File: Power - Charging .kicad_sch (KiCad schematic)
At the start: 10 parts, among them U3 MP2667GG-0000-Z

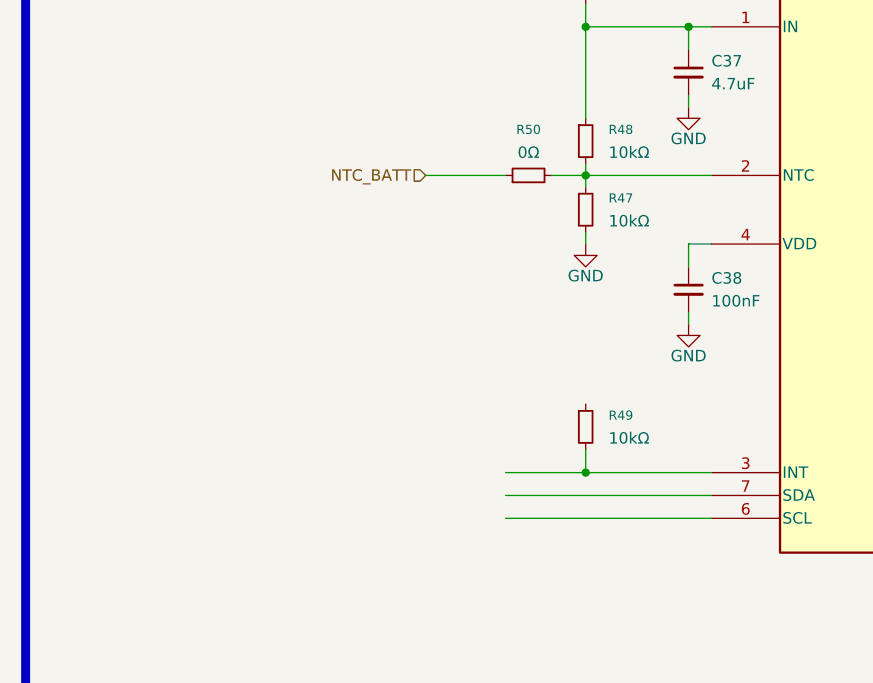
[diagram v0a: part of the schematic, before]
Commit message: charging int and i2c
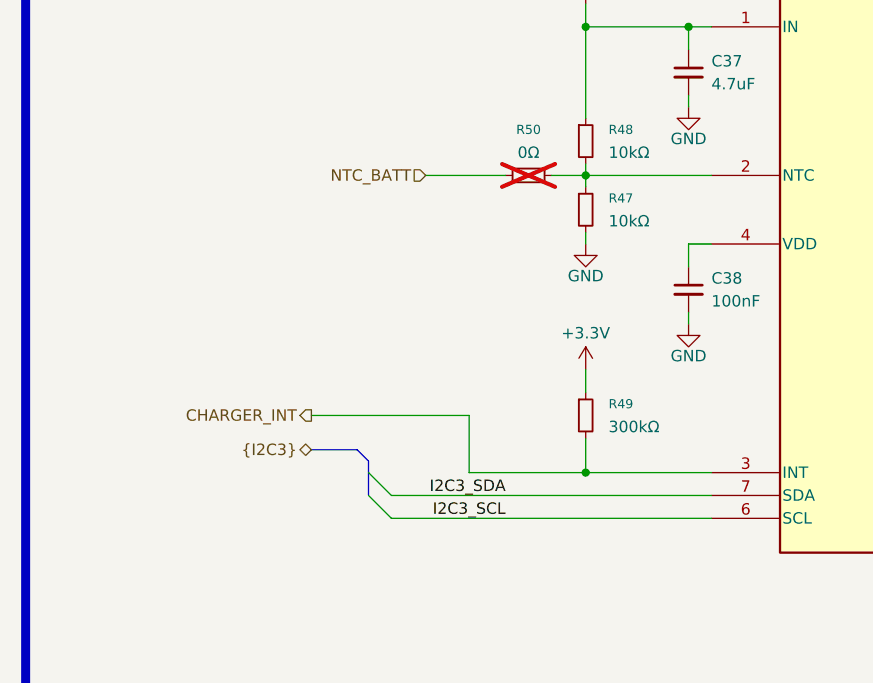
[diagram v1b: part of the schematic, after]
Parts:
- removed R49: 10kΩ, 0_resistors:R_0402_1005Metric, symbol 0_resistors:0402WGF1002TCE
- added R49: 300kΩ, 0_resistors:R_0603_1608Metric, symbol 0_resistors:0603WAF3003T5E
- R50: now not fitted; now left out of the parts list
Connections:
- net CHARGER_INT: now reaches U3.3 (INT)
- net CHARGER_INT: now also R49.2
- net I2C3_SCL: now reaches U3.6 (SCL)
- net I2C3_SDA: now reaches U3.7 (SDA)
- new net +3.3V: R49.1

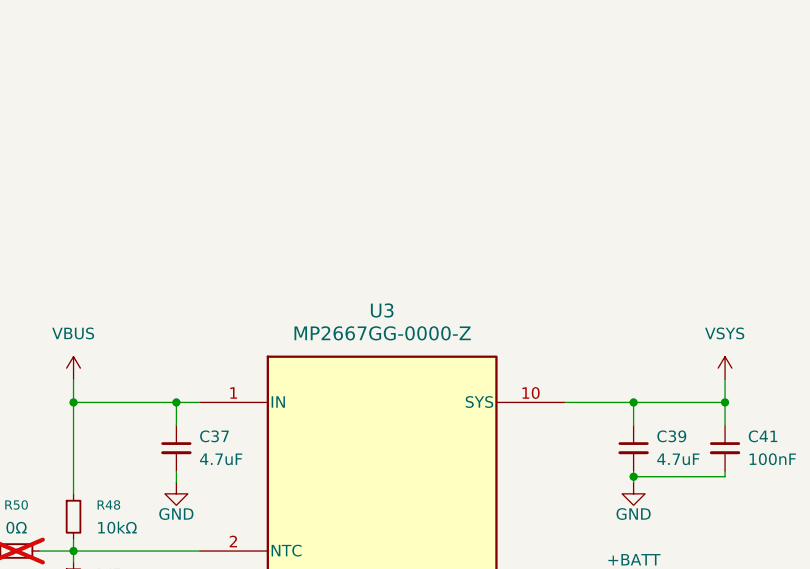
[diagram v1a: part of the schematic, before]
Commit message: added power jumper to bypass charger
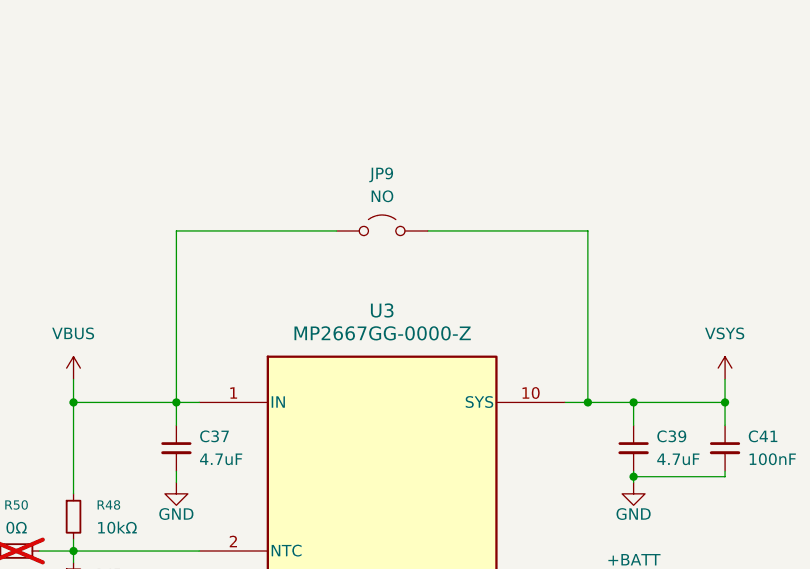
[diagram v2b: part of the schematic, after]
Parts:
- added JP9: NO, Jumper:SolderJumper-2_P1.3mm_Open_TrianglePad1.0x1.5mm, symbol 0_modules:Jumper_2_Open
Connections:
- net VBUS: now also JP9.1 (A)
- net VSYS: now also JP9.2 (B)
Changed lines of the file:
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@@
+		(color 0 0 0 0)
+	)
+	(junction
+		(at 234.95 97.79)
+		(diameter 0)
 		(color 0 0 0 0)
 	)
@@
 	(wire
 		(pts
+			(xy 234.95 78.74) (xy 234.95 97.79)
+		)
+		(stroke
+			(width 0)
+			(type default)
+		)
+	)
+	(wire
+		(pts
 			(xy 164.846 140.97) (xy 164.846 147.32)
 		)
@@
 	(wire
 		(pts
+			(xy 234.95 78.74) (xy 217.17 78.74)
+		)
+		(stroke
+			(width 0)
+			(type default)
+		)
+	)
+	(wire
+		(pts
 			(xy 177.8 114.3) (xy 177.8 115.57)
 		)
@@
 		)
 	)
+	(wire
+		(pts
+			(xy 189.23 78.74) (xy 207.01 78.74)
+		)
+		(stroke
+			(width 0)
+			(type default)
+		)
+	)
 	(bus
 		(pts
@@
 	(wire
 		(pts
+			(xy 234.95 97.79) (xy 240.03 97.79)
+		)
+		(stroke
+			(width 0)
+			(type default)
+		)
+	)
+	(wire
+		(pts
 			(xy 177.8 120.65) (xy 177.8 121.92)
 		)
@@
 	(wire
 		(pts
-			(xy 232.41 97.79) (xy 240.03 97.79)
+			(xy 232.41 97.79) (xy 234.95 97.79)
 		)
 		(stroke
@@
 		(pts
 			(xy 177.8 147.32) (xy 177.8 143.51)
+		)
+		(stroke
+			(width 0)
+			(type default)
+		)
+	)
+	(wire
+		(pts
+			(xy 189.23 78.74) (xy 189.23 97.79)
 		)
 		(stroke
@@
 					(unit 1)
 				)
+			)
+		)
+	)
+	(symbol
+		(lib_id "0_modules:Jumper_2_Open")
+		(at 212.09 78.74 0)
+		(unit 1)
+		(exclude_from_sim no)
+		(in_bom yes)
+		(on_board yes)
+		(dnp no)
+		(fields_autoplaced yes)
+		(property "Reference" "JP9"
+			(at 212.09 72.39 0)
+			(effects
+				(font
+					(size 1.27 1.27)
+				)
+			)
+		)
+		(property "Value" "NO"
+			(at 212.09 74.93 0)
+			(effects
+				(font
+					(size 1.27 1.27)
+				)
+			)
+		)
+		(property "Footprint" "Jumper:SolderJumper-2_P1.3mm_Open_TrianglePad1.0x1.5mm"
+			(at 212.09 78.74 0)
+			(effects
+				(font
+					(size 1.27 1.27)
+				)
+				(hide yes)
+			)
+		)
+		(property "Datasheet" "~"
+			(at 212.09 78.74 0)
+			(effects
+				(font
+					(size 1.27 1.27)
+				)
+				(hide yes)
+			)
+		)
+		(property "Description" "Jumper, 2-pole, open"
+			(at 212.09 78.74 0)
+			(effects
+				(font
+					(size 1.27 1.27)
+				)
+				(hide yes)
+			)
+		)
+		(pin "2"
+		)
+		(pin "1"
+		)
+		(instances
+			(project "transmitter"
+				(path "/0650c7a8-acba-429c-9f8e-eec0baf0bc1c/fede4c36-00cc-4d3d-b71c-5243ba232202/8a7ea2de-b793-4d09-a9a9-63f506951dfd"
+					(reference "JP9")
+					(unit 1)
+				)

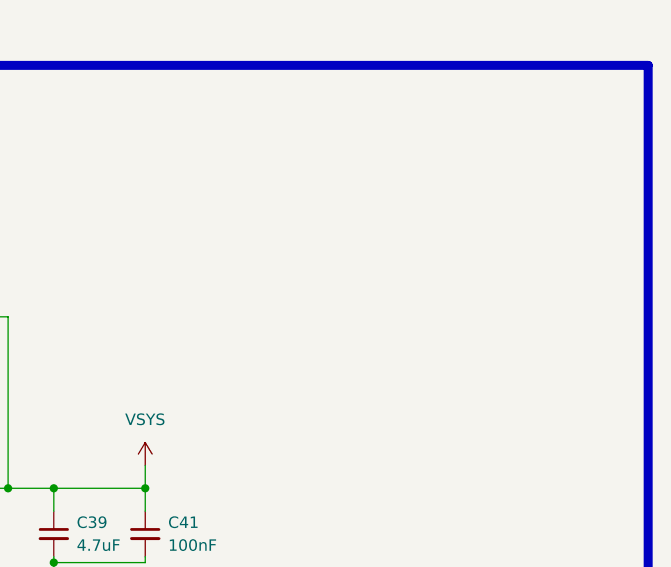
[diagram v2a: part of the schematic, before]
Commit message: added jumper to connect vbat directly to vsys
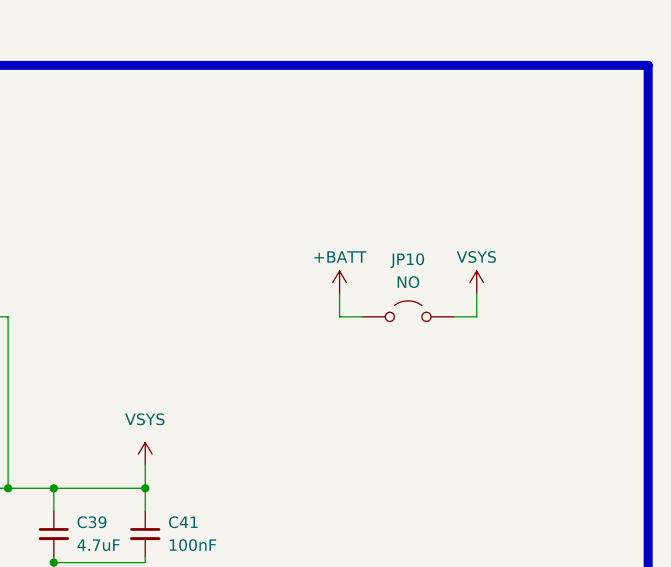
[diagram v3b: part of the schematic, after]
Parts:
- added JP10: NO, Jumper:SolderJumper-2_P1.3mm_Open_TrianglePad1.0x1.5mm, symbol 0_modules:Jumper_2_Open
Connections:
- net +BATT: now also JP10.1 (A)
- net VSYS: now also JP10.2 (B)
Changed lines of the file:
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@@
+	(wire
+		(pts
+			(xy 271.78 78.74) (xy 274.32 78.74)
+		)
+		(stroke
+			(width 0)
+			(type default)
+		)
+	)
 	(wire
 		(pts
@@
 	(wire
 		(pts
+			(xy 271.78 76.2) (xy 271.78 78.74)
+		)
+		(stroke
+			(width 0)
+			(type default)
+		)
+	)
+	(wire
+		(pts
 			(xy 240.03 123.19) (xy 240.03 127)
 		)
@@
 	(wire
 		(pts
+			(xy 287.02 76.2) (xy 287.02 78.74)
+		)
+		(stroke
+			(width 0)
+			(type default)
+		)
+	)
+	(wire
+		(pts
 			(xy 156.21 152.4) (xy 191.77 152.4)
 		)
@@
 		(pts
 			(xy 232.41 152.4) (xy 240.03 152.4)
+		)
+		(stroke
+			(width 0)
+			(type default)
+		)
+	)
+	(wire
+		(pts
+			(xy 284.48 78.74) (xy 287.02 78.74)
 		)
 		(stroke
@@
 	)
 	(symbol
+		(lib_id "0_power_symbols:VSYS")
+		(at 287.02 76.2 0)
+		(unit 1)
+		(exclude_from_sim no)
+		(in_bom yes)
+		(on_board yes)
+		(dnp no)
+		(property "Reference" "#PWR0172"
+			(at 287.02 80.01 0)
+			(effects
+				(font
+					(size 1.27 1.27)
+				)
+				(hide yes)
+			)
+		)
+		(property "Value" "VSYS"
+			(at 287.02 72.136 0)
+			(effects
+				(font
+					(size 1.27 1.27)
+				)
+			)
+		)
+		(property "Footprint" ""
+			(at 287.02 76.2 0)
+			(effects
+				(font
+					(size 1.27 1.27)
+				)
+				(hide yes)
+			)
+		)
+		(property "Datasheet" ""
+			(at 287.02 76.2 0)
+			(effects
+				(font
+					(size 1.27 1.27)
+				)
+				(hide yes)
+			)
+		)
+		(property "Description" "Power symbol creates a global label with name \"VSYS\""
+			(at 287.02 76.2 0)
+			(effects
+				(font
+					(size 1.27 1.27)
+				)
+				(hide yes)
+			)
+		)
+		(pin "1"
+		)
+		(instances
+			(project "transmitter"
+				(path "/0650c7a8-acba-429c-9f8e-eec0baf0bc1c/fede4c36-00cc-4d3d-b71c-5243ba232202/8a7ea2de-b793-4d09-a9a9-63f506951dfd"
+					(reference "#PWR0172")
+					(unit 1)
+				)
+			)
+		)
+	)
+	(symbol
 		(lib_id "0_capacitors:CL21A475KAQNNNE")
 		(at 240.03 102.87 0)
@@
 	)
 	(symbol
+		(lib_id "power:+BATT")
+		(at 271.78 76.2 0)
+		(unit 1)
+		(exclude_from_sim no)
+		(in_bom yes)
+		(on_board yes)
+		(dnp no)
+		(property "Reference" "#PWR0171"
+			(at 271.78 80.01 0)
+			(effects
+				(font
+					(size 1.27 1.27)
+				)
+				(hide yes)
+			)
+		)
+		(property "Value" "+BATT"
+			(at 271.78 72.136 0)
+			(effects
+				(font
+					(size 1.27 1.27)
+				)
+			)
+		)
+		(property "Footprint" ""
+			(at 271.78 76.2 0)
+			(effects
+				(font
+					(size 1.27 1.27)
+				)
+				(hide yes)
+			)
+		)
+		(property "Datasheet" ""
+			(at 271.78 76.2 0)
+			(effects
+				(font
+					(size 1.27 1.27)
+				)
+				(hide yes)
+			)
+		)
+		(property "Description" "Power symbol creates a global label with name \"+BATT\""
+			(at 271.78 76.2 0)
+			(effects
+				(font
+					(size 1.27 1.27)
+				)
+				(hide yes)
+			)
+		)
+		(pin "1"
+		)
+		(instances
+			(project "transmitter"
+				(path "/0650c7a8-acba-429c-9f8e-eec0baf0bc1c/fede4c36-00cc-4d3d-b71c-5243ba232202/8a7ea2de-b793-4d09-a9a9-63f506951dfd"
+					(reference "#PWR0171")
+					(unit 1)
+				)
+			)
+		)
+	)
+	(symbol
 		(lib_id "power:GND")
 		(at 177.8 121.92 0)
@@
 					(unit 1)
 				)
+			)
+		)
+	)
+	(symbol
+		(lib_id "0_modules:Jumper_2_Open")
+		(at 279.4 78.74 0)
+		(unit 1)
+		(exclude_from_sim no)
+		(in_bom yes)
+		(on_board yes)
+		(dnp no)
+		(fields_autoplaced yes)
+		(property "Reference" "JP10"
+			(at 279.4 72.39 0)
+			(effects
+				(font
+					(size 1.27 1.27)
+				)
+			)
+		)
+		(property "Value" "NO"
+			(at 279.4 74.93 0)
+			(effects
+				(font
+					(size 1.27 1.27)
+				)
+			)
+		)
+		(property "Footprint" "Jumper:SolderJumper-2_P1.3mm_Open_TrianglePad1.0x1.5mm"
+			(at 279.4 78.74 0)
+			(effects
+				(font
+					(size 1.27 1.27)
+				)
+				(hide yes)
+			)
+		)
+		(property "Datasheet" "~"
+			(at 279.4 78.74 0)
+			(effects
+				(font
+					(size 1.27 1.27)
+				)
+				(hide yes)
+			)
+		)
+		(property "Description" "Jumper, 2-pole, open"
+			(at 279.4 78.74 0)
+			(effects
+				(font
+					(size 1.27 1.27)
+				)
+				(hide yes)
+			)
+		)
+		(pin "2"
+		)
+		(pin "1"
+		)
+		(instances
+			(project "transmitter"
+				(path "/0650c7a8-acba-429c-9f8e-eec0baf0bc1c/fede4c36-00cc-4d3d-b71c-5243ba232202/8a7ea2de-b793-4d09-a9a9-63f506951dfd"
+					(reference "JP10")
+					(unit 1)
+				)

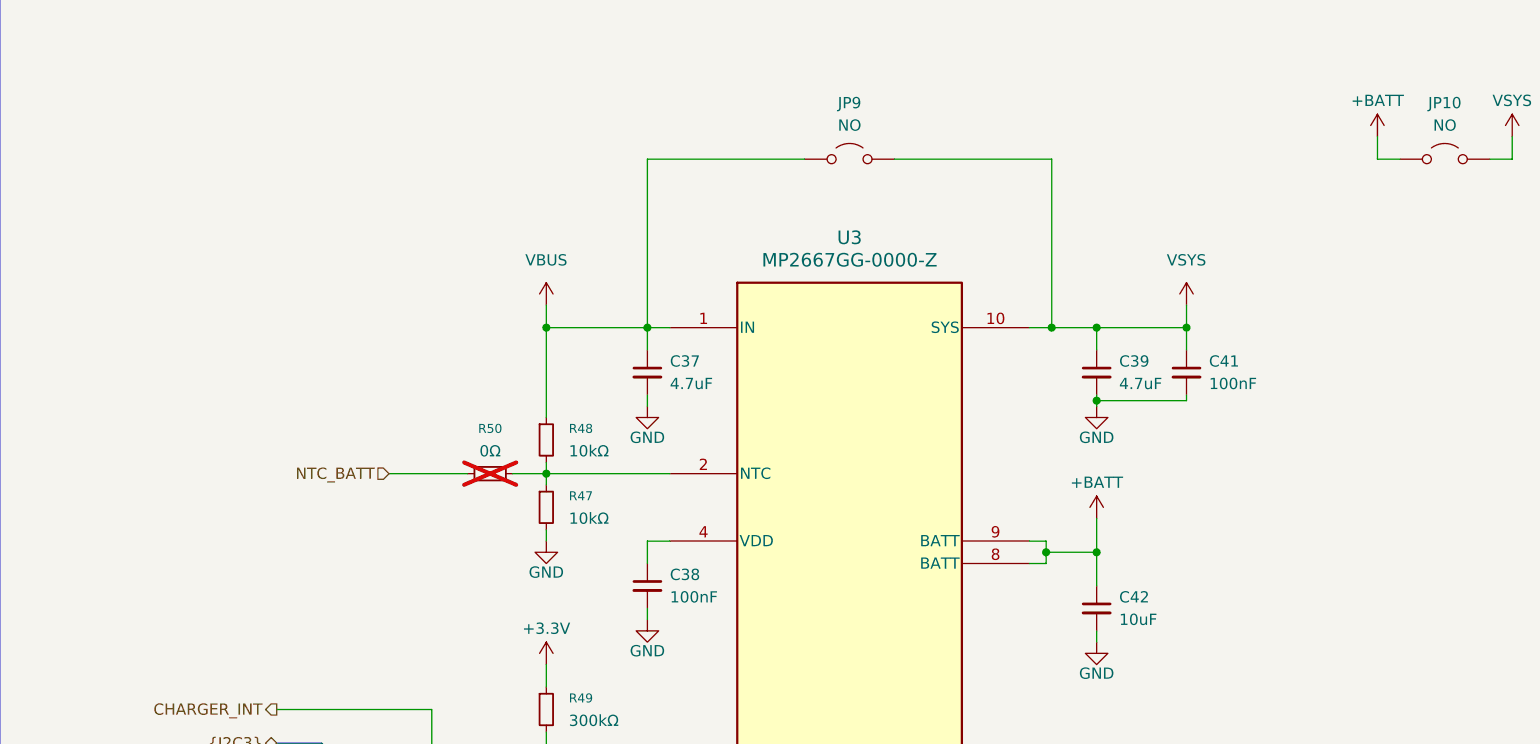
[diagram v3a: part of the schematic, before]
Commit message: duzo zmian, layout przetwornic i zasilania, wstepny routing sd card impedance control, usb differential impedance control
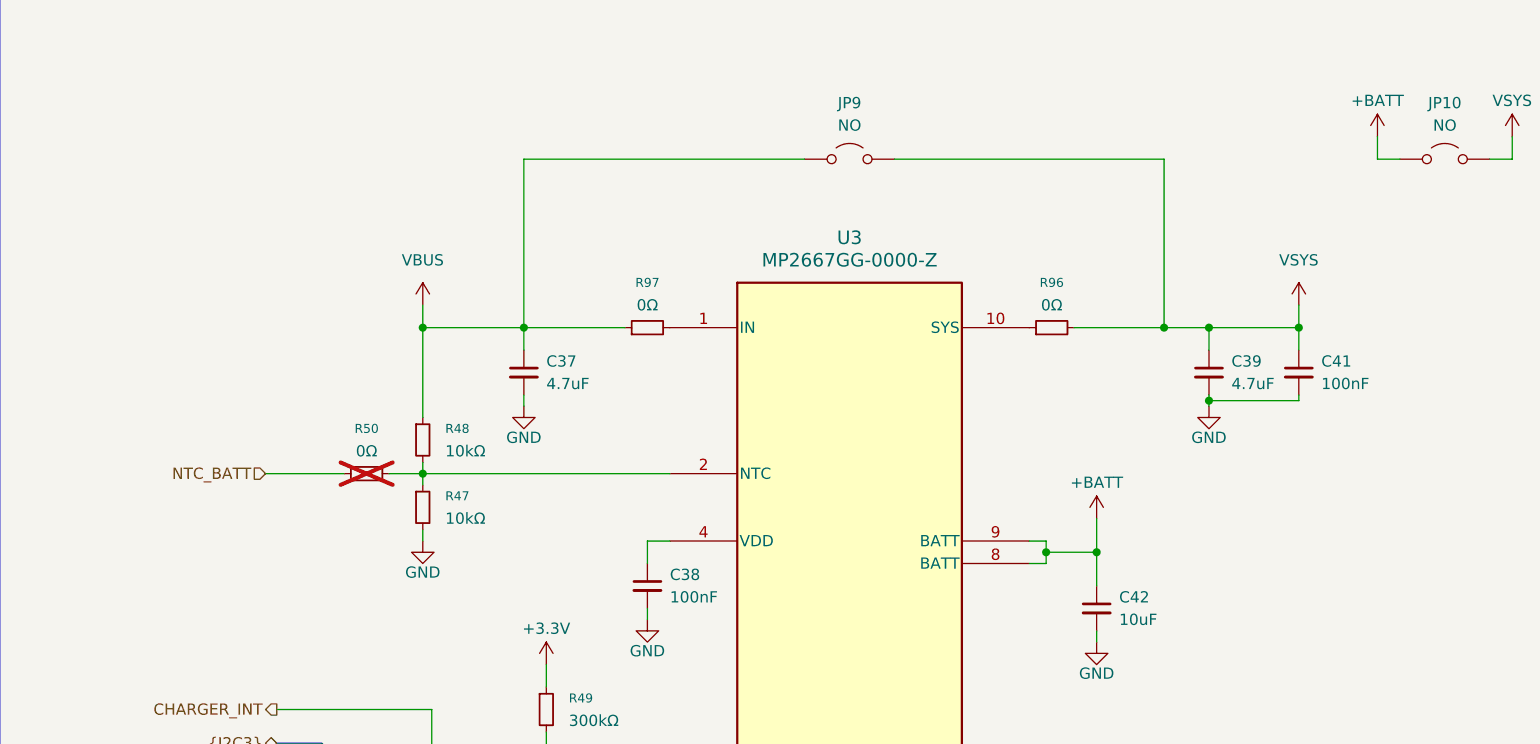
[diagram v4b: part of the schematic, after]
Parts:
- added R96, R97: 0Ω, 0_resistors:R_0402_1005Metric, symbol 0_resistors:0402WGF0000TCE
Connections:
- net VBUS: now also R97.1; no longer U3.1 (IN)
- net VSYS: now also R96.2; no longer U3.10 (SYS)
- new net: R97.2, U3.1 (IN)
- new net: R96.1, U3.10 (SYS)
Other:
- moved on the sheet: C37, C39, C41, R47, R48, R50

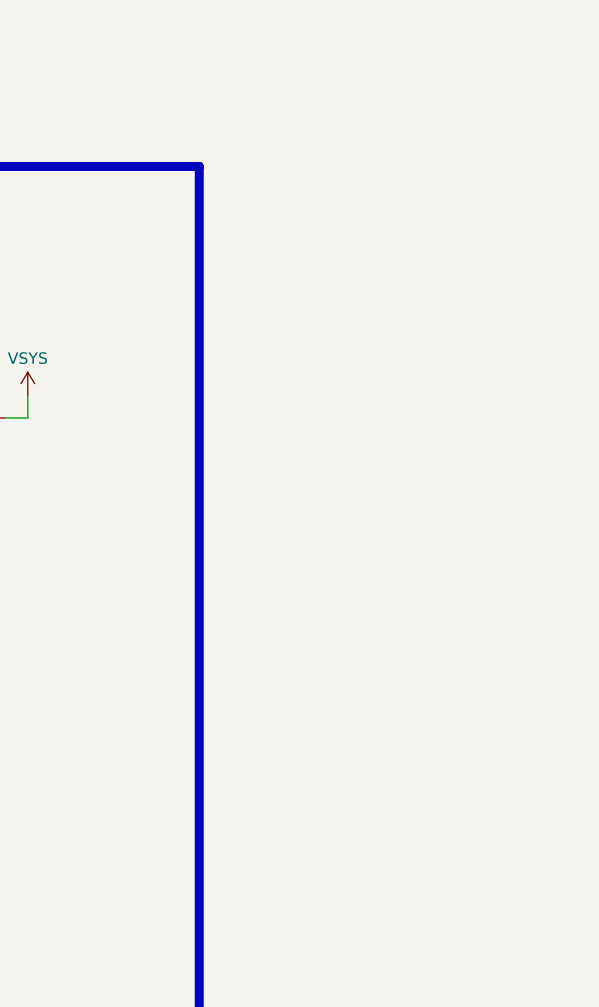
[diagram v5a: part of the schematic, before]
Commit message: added fiducal markers, mounting holes, testpoints
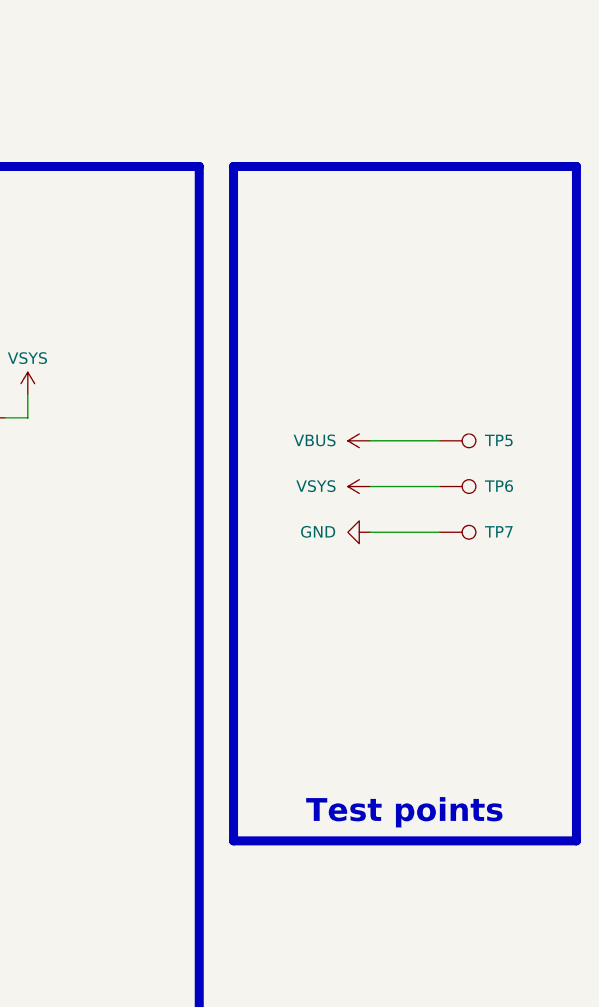
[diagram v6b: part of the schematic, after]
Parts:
- added TP5, TP6, TP7: TestPoint, 0_pads:TestPoint_Pad_D0.4mm_Back, symbol Connector:TestPoint
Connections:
- net GND: now also TP7.1
- net VBUS: now also TP5.1
- net VSYS: now also TP6.1

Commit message: test points, colors, drc
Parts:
- TP5, TP6, TP7: footprint 0_pads:TestPoint_Pad_D0.4mm_Back -> 0_pads:TestPoint_Pad_D0.5mm_Back
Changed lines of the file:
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@@
 			)
 		)
-		(property "Footprint" "0_pads:TestPoint_Pad_D0.4mm_Back"
+		(property "Footprint" "0_pads:TestPoint_Pad_D0.5mm_Back"
 			(at 332.74 91.44 0)
 			(effects
@@
 			)
 		)
-		(property "Footprint" "0_pads:TestPoint_Pad_D0.4mm_Back"
+		(property "Footprint" "0_pads:TestPoint_Pad_D0.5mm_Back"
 			(at 332.74 96.52 0)
 			(effects
@@
 			)
 		)
-		(property "Footprint" "0_pads:TestPoint_Pad_D0.4mm_Back"
+		(property "Footprint" "0_pads:TestPoint_Pad_D0.5mm_Back"
 			(at 332.74 86.36 0)
 			(effects
